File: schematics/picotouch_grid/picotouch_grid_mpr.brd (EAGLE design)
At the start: 177.8 x 111.8 mm, 188 parts, among them J1 AUDIO-JACK-TRRS, J2 AUDIO-JACK-TRRS, J3 AUDIO-JACK-TRRS, J4 STEMMA_I2C_QT, K1 TOUCHKEYH, K10 TOUCHKEYH, K11 TOUCHKEYH, K12 TOUCHKEYH, K13 TOUCHKEYH, K14 TOUCHKEYH, K15 TOUCHKEYH, K16 TOUCHKEYH, K17 TOUCHKEYH, K18 TOUCHKEYH, K19 TOUCHKEYH, K2 TOUCHKEYH, K20 TOUCHKEYH, K21 TOUCHKEYH, K22 TOUCHKEYH, K23 TOUCHKEYH, K24 TOUCHKEYH, K25 TOUCHKEYH, K26 TOUCHKEYH, K27 TOUCHKEYH, K28 TOUCHKEYH, K29 TOUCHKEYH, K3 TOUCHKEYH, K30 TOUCHKEYH, K31 TOUCHKEYH, K32 TOUCHKEYH, K33 TOUCHKEYH, K34 TOUCHKEYH, K35 TOUCHKEYH, K36 TOUCHKEYH, K37 TOUCHKEYH, K38 TOUCHKEYH, K39 TOUCHKEYH, K4 TOUCHKEYH, K40 TOUCHKEYH, K5 TOUCHKEYH, K6 TOUCHKEYH, K7 TOUCHKEYH, K8 TOUCHKEYH, K9 TOUCHKEYH, U1 RASPBERRY_PICO, U2 MPR121, U3 MPR121, U4 MPR121, U5 MPR121, U6 H11L1MS, U7 ADAFRUIT_QTPY_BFF

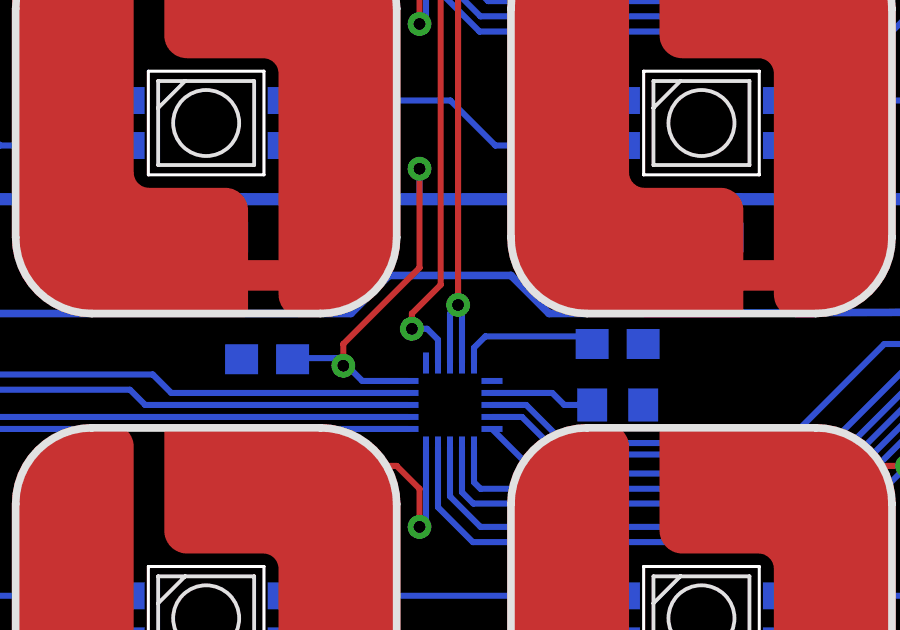
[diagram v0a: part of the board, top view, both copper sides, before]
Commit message: move confusing research code to research dir
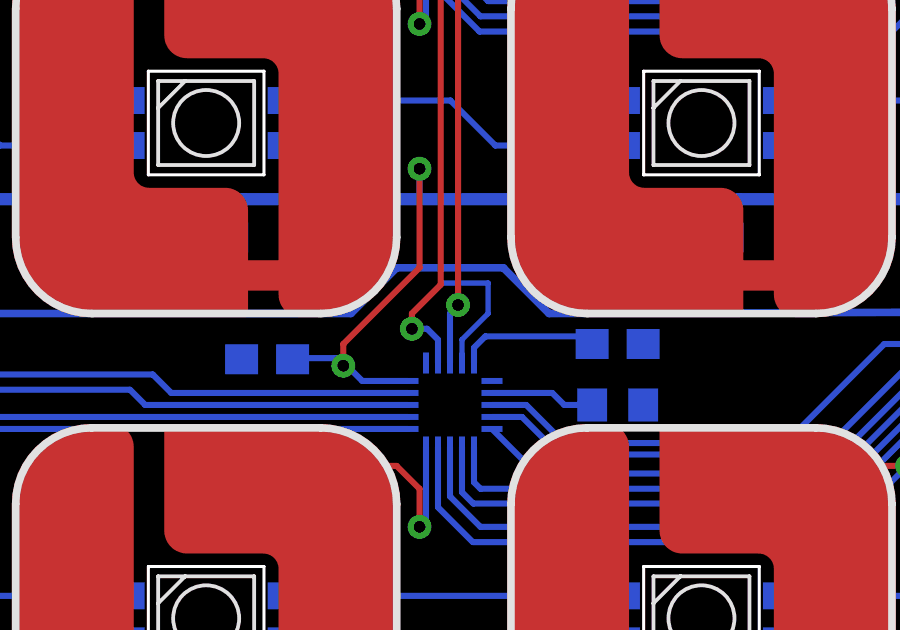
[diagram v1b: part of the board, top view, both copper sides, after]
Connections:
- net SCL: now also U5.4
- net SDA: no longer U5.4
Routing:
- net SCL: track 167.4 -> 173.9 mm
- net SDA: track 177.1 -> 175.1 mm
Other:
- board text added: "https://github.com/todbot/picotouch - 7 Apr 2023 - @todbot"
- board text removed: "https://github.com/todbot/picotouch - 27 Mar 2023 - @todbot"
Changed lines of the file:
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@@
 <grid distance="0.05" unitdist="inch" unit="inch" style="lines" multiple="1" display="no" altdistance="0.01" altunitdist="inch" altunit="inch"/>
 <layers>
-<layer number="1" name="Top" color="4" fill="1" visible="no" active="yes"/>
+<layer number="1" name="Top" color="4" fill="1" visible="yes" active="yes"/>
 <layer number="2" name="Route2" color="16" fill="1" visible="no" active="no"/>
 <layer number="3" name="Route3" color="17" fill="1" visible="no" active="no"/>
@@
   capsense touch grid keyboard
   for Raspberry Pi Pico</text>
-<text x="82.55" y="2.54" size="1.778" layer="22" ratio="12" rot="MR0">https://github.com/todbot/picotouch - 27 Mar 2023 - @todbot</text>
+<text x="82.55" y="2.54" size="1.778" layer="22" ratio="12" rot="MR0">https://github.com/todbot/picotouch - 7 Apr 2023 - @todbot</text>
 <text x="149.86" y="2.54" size="1.778" layer="26" rot="MR0">JLCJLCJLCJLC</text>
 <text x="135.636" y="81.28" size="1.016" layer="22" ratio="10" rot="MR0" align="top-left">optional I2C OLED display
@@
 <wire x1="83.928" y1="21.212" x2="83.928" y2="21.99" width="0.2032" layer="16"/>
 <wire x1="83.928" y1="21.99" x2="83.565996875" y2="22.352003125" width="0.2032" layer="16"/>
-<wire x1="83.565996875" y1="22.352003125" x2="83.058" y2="22.352" width="0.2032" layer="16"/>
+<wire x1="83.565996875" y1="22.352003125" x2="83.058003125" y2="22.352" width="0.2032" layer="16"/>
 <via x="83.058" y="22.352" extent="1-16" drill="0.3937"/>
+<wire x1="83.058003125" y1="22.352" x2="83.058" y2="22.352" width="0.2032" layer="16"/>
 <wire x1="84.018471875" y1="39.171528125" x2="84.018471875" y2="38.663528125" width="0.2032" layer="1"/>
 <wire x1="84.018471875" y1="38.663528125" x2="84.018471875" y2="23.820471875" width="0.2032" layer="1"/>
@@
 <wire x1="96.844" y1="101.53" x2="98.552" y2="99.822" width="0.2032" layer="16"/>
 <wire x1="98.552" y1="99.822" x2="98.552" y2="91.694" width="0.2032" layer="16"/>
+<contactref element="U5" pad="4"/>
+<wire x1="84.728" y1="21.212" x2="84.728" y2="21.99" width="0.1778" layer="16"/>
+<wire x1="85.598" y1="22.86" x2="85.598" y2="23.876" width="0.1778" layer="16"/>
+<wire x1="85.598" y1="23.876" x2="84.074" y2="23.876" width="0.1778" layer="16"/>
+<wire x1="84.074" y1="23.876" x2="83.058003125" y2="22.860003125" width="0.1778" layer="16"/>
+<wire x1="83.058003125" y1="22.860003125" x2="83.058003125" y2="22.352" width="0.1778" layer="16"/>
+<wire x1="84.728" y1="21.99" x2="85.598" y2="22.86" width="0.1778" layer="16"/>
 </signal>
 <signal name="SDA">
@@
 <wire x1="84.596625" y1="23.14575" x2="84.596625" y2="39.057378125" width="0.2032" layer="1"/>
 <wire x1="84.328" y1="38.5888125" x2="84.728" y2="38.9888125" width="0.2032" layer="16"/>
-<contactref element="U5" pad="4"/>
 <contactref element="U5" pad="3"/>
 <wire x1="84.328" y1="21.212" x2="84.328" y2="22.86" width="0.2032" layer="16"/>
@@
 <via x="84.596625" y="23.14575" extent="1-16" drill="0.3937"/>
 <wire x1="84.328" y1="22.86" x2="84.596625" y2="23.128625" width="0.2032" layer="16"/>
-<wire x1="84.728" y1="21.212" x2="84.728" y2="22.99725" width="0.2032" layer="16"/>
-<wire x1="84.728" y1="22.99725" x2="84.596625" y2="23.128625" width="0.2032" layer="16"/>
 <contactref element="R6" pad="2"/>
 <wire x1="84.596625" y1="73.674625" x2="84.596625" y2="73.152" width="0.2032" layer="1"/>
@@
 <contactref element="LED30" pad="2-DOUT"/>
 <wire x1="163.83" y1="23.114" x2="87.63" y2="22.86" width="0.254" layer="16"/>
-<wire x1="87.63" y1="22.86" x2="86.36" y2="24.13" width="0.254" layer="16"/>
-<wire x1="86.36" y1="24.13" x2="82.296" y2="24.13" width="0.254" layer="16"/>
-<wire x1="82.296" y1="24.13" x2="81.026" y2="22.86" width="0.254" layer="16"/>
+<wire x1="87.63" y1="22.86" x2="86.106" y2="24.384" width="0.254" layer="16"/>
+<wire x1="86.106" y1="24.384" x2="82.55" y2="24.384" width="0.254" layer="16"/>
+<wire x1="82.55" y1="24.384" x2="81.026" y2="22.86" width="0.254" layer="16"/>
 <wire x1="81.026" y1="22.86" x2="5.08" y2="22.86" width="0.254" layer="16"/>
 <wire x1="2.54" y1="12.7" x2="3.29" y2="11.95" width="0.254" layer="16"/>
